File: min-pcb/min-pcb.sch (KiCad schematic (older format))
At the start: 5 parts, among them J1 Conn_Pi, J2 Conn_DCDC, SW1 SW_Push, U1 74HCT74

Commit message: Rev1
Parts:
- added J3: Conn_Ext_Btn, Connector_PinHeader_2.54mm:PinHeader_1x02_P2.54mm_Horizontal, symbol Connector:Conn_01x02_Male
- J1: footprint (none) -> Connector_PinHeader_2.54mm:PinHeader_1x04_P2.54mm_Horizontal; symbol Connector:Conn_01x03_Male -> Connector:Conn_01x04_Male
- J2: footprint (none) -> Connector_PinHeader_2.54mm:PinHeader_1x05_P2.54mm_Horizontal; symbol Connector:Conn_01x04_Male -> Connector:Conn_01x05_Male
- R1: footprint (none) -> Resistor_THT:R_Axial_DIN0207_L6.3mm_D2.5mm_P7.62mm_Horizontal
- SW1: footprint (none) -> Button_Switch_THT:SW_PUSH_6mm_H9.5mm
- U1: footprint digikey-footprints:DIP-14_W3mm -> Package_DIP:DIP-14_W7.62mm_Socket
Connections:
- net +5V: now also J1.3 (Pin_3), J2.4 (Pin_4); no longer J1.2 (Pin_2), J2.3 (Pin_3)
- net En: now also J2.5 (Pin_5); no longer J2.4 (Pin_4)
- net GND: now also J1.1 (Pin_1), J2.3 (Pin_3), J3.1 (Pin_1); no longer J1.3 (Pin_3), J2.2 (Pin_2)
- net GPIO26: now also J1.4 (Pin_4); no longer J1.1 (Pin_1)
- net Vin: now also J2.2 (Pin_2); no longer J2.1 (Pin_1)
- net at R1.1, SW1.2, U1.4 (1~PRE): now also J3.2 (Pin_2)
- new net LBO: J1.2 (Pin_2), J2.1 (Pin_1)
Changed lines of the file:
@@
 encoding utf-8
 Sheet 1 1
-Title ""
-Date ""
-Rev ""
-Comp ""
-Comment1 ""
+Title "Pi Battery Management"
+Date "2020-09-22"
+Rev "1"
+Comp "Bernhard Bablok"
+Comment1 "https://github.com/bablokb/pcb-pi-batman"
 Comment2 ""
 Comment3 ""
@@
 F 0 "R1" V 3950 3900 50  0000 C CNN
 F 1 "10K" V 3850 3900 50  0000 C CNN
-F 2 "" V 3780 3900 50  0001 C CNN
+F 2 "Resistor_THT:R_Axial_DIN0207_L6.3mm_D2.5mm_P7.62mm_Horizontal" V 3780 3900 50  0001 C CNN
 F 3 "~" H 3850 3900 50  0001 C CNN
 	1    3850 3900
@@
 $EndComp
 $Comp
-L Connector:Conn_01x04_Male J2
+L Connector:Conn_01x05_Male J2
 U 1 1 5F54C963
 P 6400 4150
 F 0 "J2" H 6500 4400 50  0000 R CNN
 F 1 "Conn_DCDC" H 6600 4500 50  0000 R CNN
-F 2 "" H 6400 4150 50  0001 C CNN
+F 2 "Connector_PinHeader_2.54mm:PinHeader_1x05_P2.54mm_Horizontal" H 6400 4150 50  0001 C CNN
 F 3 "~" H 6400 4150 50  0001 C CNN
 	1    6400 4150
@@
 $EndComp
 $Comp
-L power:GND #PWR0101
-U 1 1 5F551E8D
-P 3750 4400
-F 0 "#PWR0101" H 3750 4150 50  0001 C CNN
-F 1 "GND" V 3755 4272 50  0000 R CNN
-F 2 "" H 3750 4400 50  0001 C CNN
-F 3 "" H 3750 4400 50  0001 C CNN
-	1    3750 4400
-	0    1    1    0
-$EndComp
-$Comp
 L temp:SN74HC74N U1
 U 1 1 5F65EDBD
@@
 F 0 "U1" H 5000 4603 60  0000 C CNN
 F 1 "74HCT74" H 5000 4497 60  0000 C CNN
-F 2 "digikey-footprints:DIP-14_W3mm" H 5250 4100 60  0001 L CNN
+F 2 "Package_DIP:DIP-14_W7.62mm_Socket" H 5250 4100 60  0001 L CNN
 F 3 "http://www.ti.com/general/docs/suppproductinfo.tsp?distId=10&gotoUrl=http%3A%2F%2Fwww.ti.com%2Flit%2Fgpn%2Fsn74hc74" H 5250 4200 60  0001 L CNN
 F 4 "296-1602-5-ND" H 5250 4300 60  0001 L CNN "Digi-Key_PN"
@@
 U 1 1 5F54A71C
 P 3950 4400
-F 0 "SW1" H 3900 4200 50  0000 C CNN
-F 1 "SW_Push" H 3900 4300 50  0000 C CNN
-F 2 "" H 3950 4600 50  0001 C CNN
+F 0 "SW1" H 3700 4600 50  0000 C CNN
+F 1 "SW_Push" H 3650 4500 50  0000 C CNN
+F 2 "Button_Switch_THT:SW_PUSH_6mm_H9.5mm" H 3950 4600 50  0001 C CNN
 F 3 "~" H 3950 4600 50  0001 C CNN
 	1    3950 4400
@@
 	6800 3550 6800 3400
 $Comp
-L Connector:Conn_01x03_Male J1
+L Connector:Conn_01x04_Male J1
 U 1 1 5F54A0B2
-P 2950 3850
-F 0 "J1" H 2800 3950 50  0000 C CNN
-F 1 "Conn_Pi" H 2750 3800 50  0000 C CNN
-F 2 "" H 2950 3850 50  0001 C CNN
-F 3 "~" H 2950 3850 50  0001 C CNN
-	1    2950 3850
-	-1   0    0    -1
+P 2950 3950
+F 0 "J1" H 2800 4050 50  0000 C CNN
+F 1 "Conn_Pi" H 2750 3900 50  0000 C CNN
+F 2 "Connector_PinHeader_2.54mm:PinHeader_1x04_P2.54mm_Horizontal" H 2950 3950 50  0001 C CNN
+F 3 "~" H 2950 3950 50  0001 C CNN
+	1    2950 3950
+	-1   0    0    1
 $EndComp
 Text Label 2750 3850 2    50   ~ 0
 +5V
-Wire Wire Line
-	2750 3600 2750 3750
-Wire Wire Line
-	2750 3950 2750 5050
 Wire Wire Line
 	2750 5050 5150 5050
@@
 Text Label 2750 3750 2    50   ~ 0
 GPIO26
+Text Label 6600 4350 0    50   ~ 0
+LBO
+Wire Wire Line
+	2750 5050 2750 4400
+Text Label 2750 3950 2    50   ~ 0
+LBO
+$Comp
+L Connector:Conn_01x02_Male J3
+U 1 1 5F6A3547
+P 3900 4950
+F 0 "J3" V 4050 5300 50  0000 R CNN
+F 1 "Conn_Ext_Btn" V 3950 5550 50  0000 R CNN
+F 2 "Connector_PinHeader_2.54mm:PinHeader_1x02_P2.54mm_Horizontal" H 3900 4950 50  0001 C CNN
+F 3 "~" H 3900 4950 50  0001 C CNN
+	1    3900 4950
+	0    -1   -1   0
+$EndComp
+Wire Wire Line
+	4000 4750 4150 4750
+Wire Wire Line
+	4150 4750 4150 4400
+Connection ~ 4150 4400
+Wire Wire Line
+	3900 4750 3750 4750
+Wire Wire Line
+	3750 4750 3750 4400
+Wire Wire Line
+	3750 4400 2750 4400
+Connection ~ 3750 4400
+Connection ~ 2750 4400
+Wire Wire Line
+	2750 4400 2750 4050
+Wire Wire Line
+	2750 3600 2750 3750
 $EndSCHEMATC

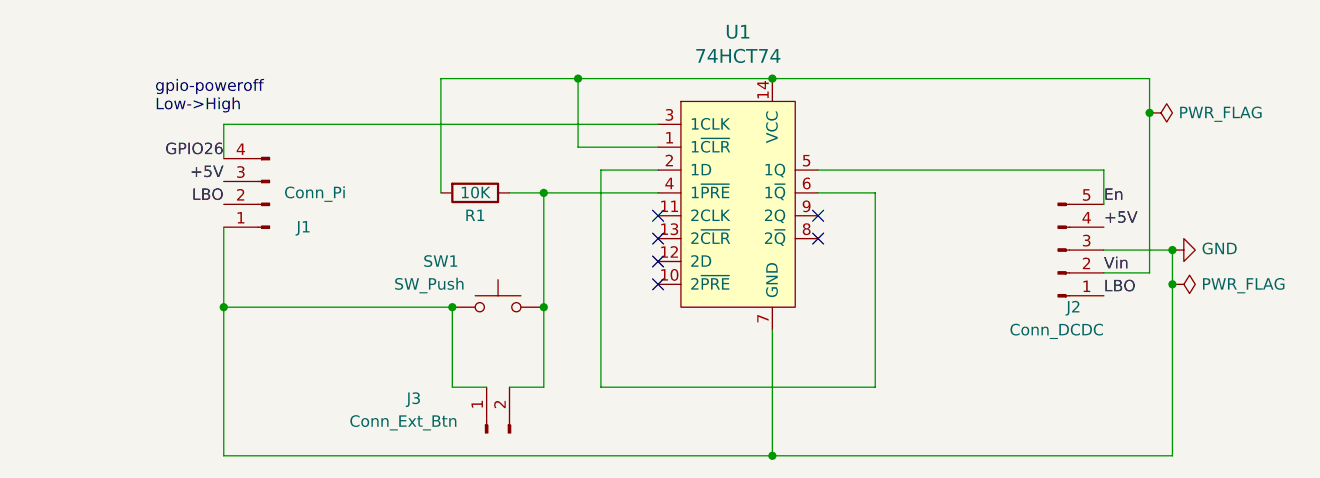
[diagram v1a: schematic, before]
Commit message: rearranged pins on connectors
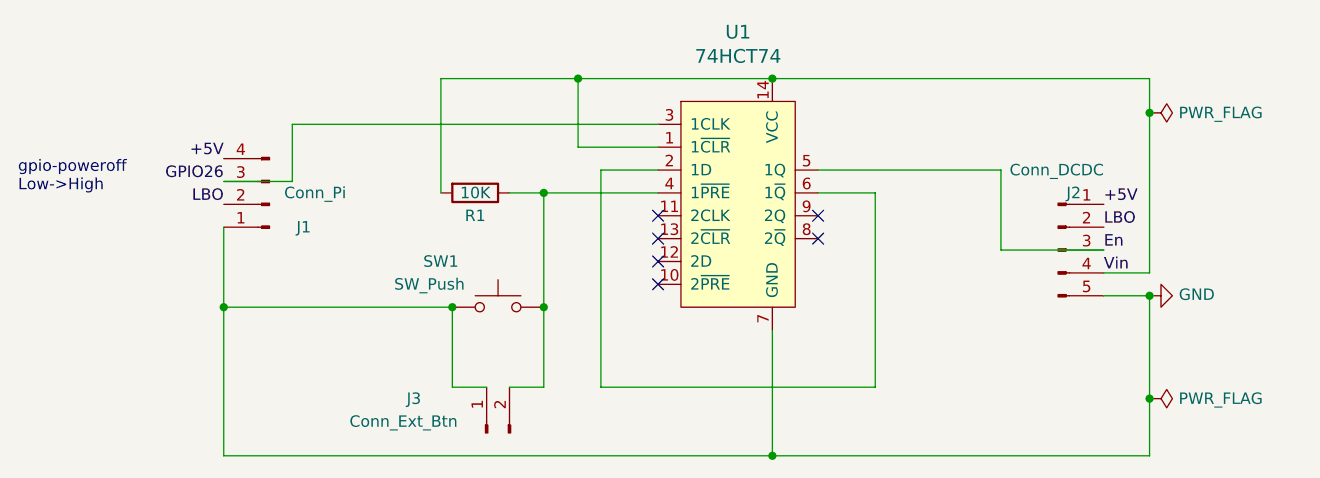
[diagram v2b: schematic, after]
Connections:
- net +5V: now also J1.4 (Pin_4), J2.1 (Pin_1); no longer J1.3 (Pin_3), J2.4 (Pin_4)
- net En: now also J2.3 (Pin_3); no longer J2.5 (Pin_5)
- net GND: now also J2.5 (Pin_5); no longer J2.3 (Pin_3)
- net GPIO26: now also J1.3 (Pin_3); no longer J1.4 (Pin_4)
- net LBO: now also J2.2 (Pin_2); no longer J2.1 (Pin_1)
- net Vin: now also J2.4 (Pin_4); no longer J2.2 (Pin_2)
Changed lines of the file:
@@
 F 3 "~" H 6400 4150 50  0001 C CNN
 	1    6400 4150
-	1    0    0    1
+	1    0    0    -1
 $EndComp
 $Comp
 L power:GND #PWR02
 U 1 1 5F54DE0D
-P 6900 4150
-F 0 "#PWR02" H 6900 3900 50  0001 C CNN
-F 1 "GND" V 6905 4022 50  0000 R CNN
-F 2 "" H 6900 4150 50  0001 C CNN
-F 3 "" H 6900 4150 50  0001 C CNN
-	1    6900 4150
+P 6800 4350
+F 0 "#PWR02" H 6800 4100 50  0001 C CNN
+F 1 "GND" V 6805 4222 50  0000 R CNN
+F 2 "" H 6800 4350 50  0001 C CNN
+F 3 "" H 6800 4350 50  0001 C CNN
+	1    6800 4350
 	0    -1   -1   0
 $EndComp
@@
 	1    0    0    -1
 $EndComp
-Text Notes 2450 3550 0    50   ~ 0
+Text Notes 1850 3900 0    50   ~ 0
 gpio-poweroff\nLow->High
 $Comp
@@
 L power:PWR_FLAG #FLG0102
 U 1 1 5F66B4BA
-P 6900 4300
-F 0 "#FLG0102" H 6900 4375 50  0001 C CNN
-F 1 "PWR_FLAG" V 6900 4427 50  0000 L CNN
-F 2 "" H 6900 4300 50  0001 C CNN
-F 3 "~" H 6900 4300 50  0001 C CNN
-	1    6900 4300
+P 6800 4800
+F 0 "#FLG0102" H 6800 4875 50  0001 C CNN
+F 1 "PWR_FLAG" V 6800 4927 50  0000 L CNN
+F 2 "" H 6800 4800 50  0001 C CNN
+F 3 "~" H 6800 4800 50  0001 C CNN
+	1    6800 4800
 	0    1    1    0
 $EndComp
@@
 Wire Wire Line
 	4150 3900 4650 3900
-Wire Wire Line
-	2750 3600 4650 3600
 Text Label 6600 4250 0    50   ~ 0
 Vin
-Text Label 6600 4050 0    50   ~ 0
+Text Label 6600 3950 0    50   ~ 0
 +5V
-Text Label 6600 3950 0    50   ~ 0
+Text Label 6600 4150 0    50   ~ 0
 En
 Wire Wire Line
-	6600 4150 6900 4150
-Wire Wire Line
-	6900 4150 6900 4300
-Wire Wire Line
-	6900 5050 5150 5050
-Connection ~ 6900 4150
-Connection ~ 6900 4300
-Wire Wire Line
-	6900 4300 6900 5050
-Wire Wire Line
 	5150 4500 5150 5050
-Wire Wire Line
-	6600 3800 6600 3950
-Wire Wire Line
-	5350 3800 6600 3800
 Wire Wire Line
 	6600 4250 6800 4250
@@
 	-1   0    0    1
 $EndComp
-Text Label 2750 3850 2    50   ~ 0
+Text Label 2750 3750 2    50   ~ 0
 +5V
 Wire Wire Line
 	2750 5050 5150 5050
-Connection ~ 5150 5050
-Text Label 2750 3750 2    50   ~ 0
+Text Label 2750 3850 2    50   ~ 0
 GPIO26
-Text Label 6600 4350 0    50   ~ 0
+Text Label 6600 4050 0    50   ~ 0
 LBO
 Wire Wire Line
@@
 Wire Wire Line
 	2750 4400 2750 4050
+Connection ~ 6800 4350
 Wire Wire Line
-	2750 3600 2750 3750
+	6800 4350 6800 4800
+Wire Wire Line
+	6600 4350 6800 4350
+Wire Wire Line
+	5350 3800 6150 3800
+Wire Wire Line
+	6150 3800 6150 4150
+Wire Wire Line
+	6150 4150 6600 4150
+Wire Wire Line
+	6800 5050 5150 5050
+Wire Wire Line
+	6800 4800 6800 5050
+Connection ~ 6800 4800
+Connection ~ 5150 5050
+Wire Wire Line
+	4650 3600 3050 3600
+Wire Wire Line
+	3050 3600 3050 3850
+Wire Wire Line
+	3050 3850 2750 3850
 $EndSCHEMATC

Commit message: Rev2: added power to external connector, added mounting-holes
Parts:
- J3: value Conn_Ext_Btn -> Conn_Ext; footprint Connector_PinHeader_2.54mm:PinHeader_1x02_P2.54mm_Horizontal -> Connector_PinHeader_2.54mm:PinHeader_1x03_P2.54mm_Horizontal; symbol Connector:Conn_01x02_Male -> Connector:Conn_01x03_Male
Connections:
- net Vin: now also J3.2 (Pin_2)
- net at R1.1, SW1.2, U1.4 (1~PRE): now also J3.3 (Pin_3); no longer J3.2 (Pin_2)
- net GPIO26 renamed GPIOxx
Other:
- note added: "off: Low->High\n(gpio-poweroff)\n"
- note added: "on: High -> Low"
- note removed: "gpio-poweroff\nLow->High"
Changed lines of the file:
@@
 Sheet 1 1
 Title "Pi Battery Management"
-Date "2020-09-22"
-Rev "1"
+Date "2020-09-23"
+Rev "2"
 Comp "Bernhard Bablok"
 Comment1 "https://github.com/bablokb/pcb-pi-batman"
@@
 	1    0    0    -1
 $EndComp
-Text Notes 1850 3900 0    50   ~ 0
-gpio-poweroff\nLow->High
+Text Notes 2000 3900 0    39   ~ 0
+off: Low->High\n(gpio-poweroff)\n
 $Comp
 L power:PWR_FLAG #FLG0101
@@
 	2750 5050 5150 5050
 Text Label 2750 3850 2    50   ~ 0
-GPIO26
+GPIOxx
 Text Label 6600 4050 0    50   ~ 0
 LBO
@@
 LBO
 $Comp
-L Connector:Conn_01x02_Male J3
+L Connector:Conn_01x03_Male J3
 U 1 1 5F6A3547
 P 3900 4950
 F 0 "J3" V 4050 5300 50  0000 R CNN
-F 1 "Conn_Ext_Btn" V 3950 5550 50  0000 R CNN
-F 2 "Connector_PinHeader_2.54mm:PinHeader_1x02_P2.54mm_Horizontal" H 3900 4950 50  0001 C CNN
+F 1 "Conn_Ext" V 3950 5550 50  0000 R CNN
+F 2 "Connector_PinHeader_2.54mm:PinHeader_1x03_P2.54mm_Horizontal" H 3900 4950 50  0001 C CNN
 F 3 "~" H 3900 4950 50  0001 C CNN
 	1    3900 4950
@@
 Connection ~ 4150 4400
 Wire Wire Line
-	3900 4750 3750 4750
-Wire Wire Line
 	3750 4750 3750 4400
 Wire Wire Line
@@
 Wire Wire Line
 	3050 3850 2750 3850
+Wire Wire Line
+	3750 4750 3800 4750
+Wire Wire Line
+	3900 4750 3900 4650
+Text Notes 3200 4500 0    39   ~ 0
+on: High -> Low
+Text Label 3900 4650 0    50   ~ 0
+Vin
 $EndSCHEMATC

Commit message: replaced 74HCT74 with 74HC74
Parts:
- U1: value 74HCT74 -> 74HC74; symbol temp:SN74HC74N -> User:SN74HC74N
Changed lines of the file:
@@
 Sheet 1 1
 Title "Pi Battery Management"
-Date "2020-09-23"
-Rev "2"
+Date "2020-10-12"
+Rev "3"
 Comp "Bernhard Bablok"
 Comment1 "https://github.com/bablokb/pcb-pi-batman"
@@
 $EndComp
 $Comp
-L temp:SN74HC74N U1
+L User:SN74HC74N U1
 U 1 1 5F65EDBD
 P 5050 3900
 F 0 "U1" H 5000 4603 60  0000 C CNN
-F 1 "74HCT74" H 5000 4497 60  0000 C CNN
+F 1 "74HC74" H 5000 4497 60  0000 C CNN
 F 2 "Package_DIP:DIP-14_W7.62mm_Socket" H 5250 4100 60  0001 L CNN
 F 3 "http://www.ti.com/general/docs/suppproductinfo.tsp?distId=10&gotoUrl=http%3A%2F%2Fwww.ti.com%2Flit%2Fgpn%2Fsn74hc74" H 5250 4200 60  0001 L CNN

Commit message: bugfix: prevent 2nd flip-flop from floating
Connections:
- net GND: now also U1.11 (2CLK), U1.12 (2D)
- net Vin: now also U1.10 (2~PRE), U1.13 (2~CLR)
- no-connect marks 6 -> 2
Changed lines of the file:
@@
 Sheet 1 1
 Title "Pi Battery Management"
-Date "2020-10-12"
-Rev "3"
+Date "2020-12-15"
+Rev "4"
 Comp "Bernhard Bablok"
 Comment1 "https://github.com/bablokb/pcb-pi-batman"
@@
 NoConn ~ 5350 4000
 NoConn ~ 5350 4100
-NoConn ~ 4650 4000
-NoConn ~ 4650 4100
-NoConn ~ 4650 4200
-NoConn ~ 4650 4300
 Wire Wire Line
 	4300 3400 4300 3700
@@
 $EndComp
 Wire Wire Line
-	4300 3400 5150 3400
+	4300 3400 4500 3400
 $Comp
 L power:PWR_FLAG #FLG0102
@@
 +5V
 Wire Wire Line
-	2750 5050 5150 5050
+	2750 5050 4600 5050
 Text Label 2750 3850 2    50   ~ 0
 GPIOxx
@@
 Text Label 3900 4650 0    50   ~ 0
 Vin
+Wire Wire Line
+	4650 4100 4500 4100
+Wire Wire Line
+	4500 4100 4500 3400
+Connection ~ 4500 3400
+Wire Wire Line
+	4500 3400 5150 3400
+Wire Wire Line
+	4650 4300 4500 4300
+Wire Wire Line
+	4500 4300 4500 4100
+Connection ~ 4500 4100
+Wire Wire Line
+	4650 4200 4600 4200
+Wire Wire Line
+	4600 4200 4600 5050
+Connection ~ 4600 5050
+Wire Wire Line
+	4600 5050 5150 5050
+Wire Wire Line
+	4650 4000 4600 4000
+Wire Wire Line
+	4600 4000 4600 4200
+Connection ~ 4600 4200
 $EndSCHEMATC
